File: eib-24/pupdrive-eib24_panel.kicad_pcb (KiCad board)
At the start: 2 copper layers, 125 x 110 mm, 454 parts, among them J1 050702422, J2 050702422

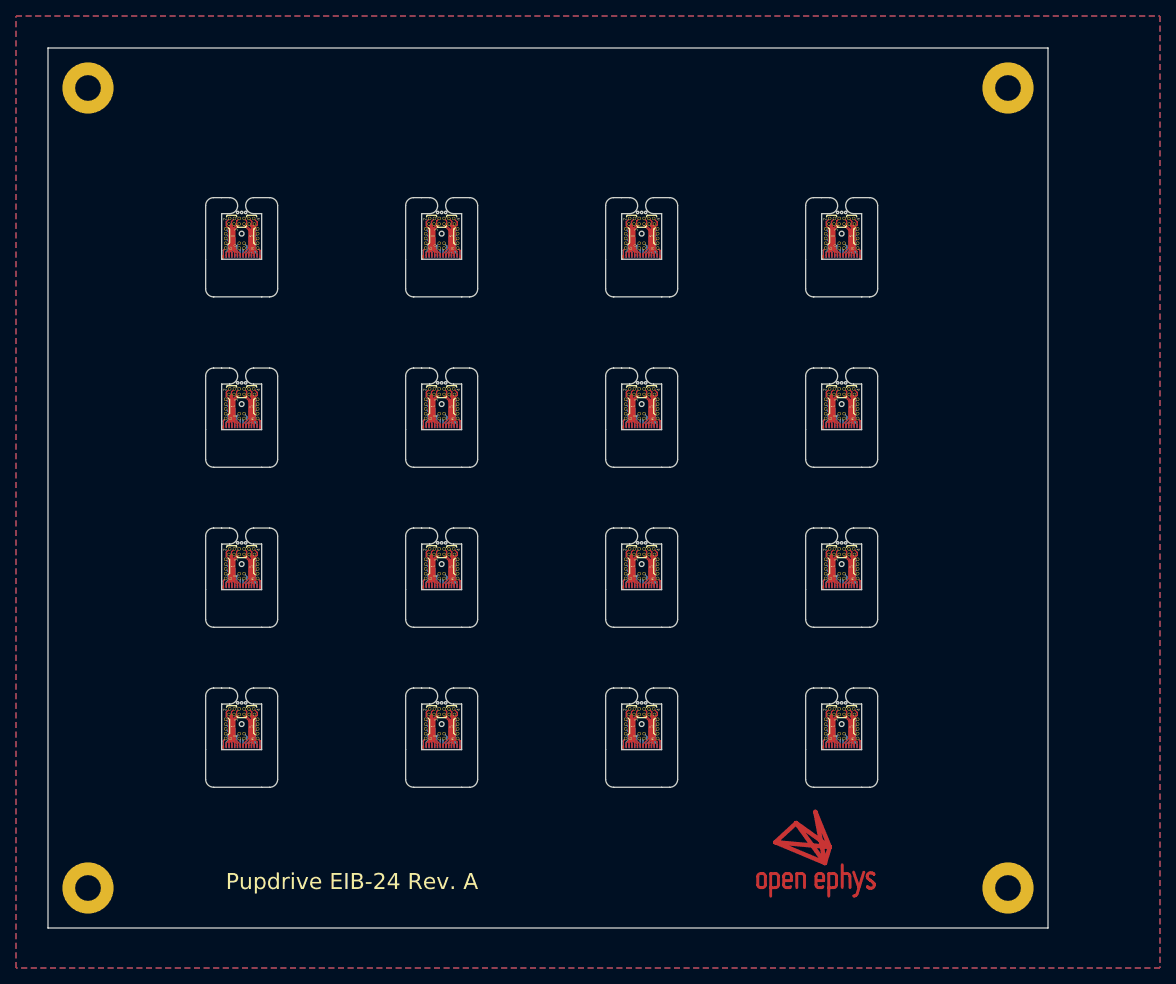
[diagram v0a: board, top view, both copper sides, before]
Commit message: Changes following first real-world test
- EIB revision B that allows it to be screwed into EIB holder for
assembly
- Small changes to drive design
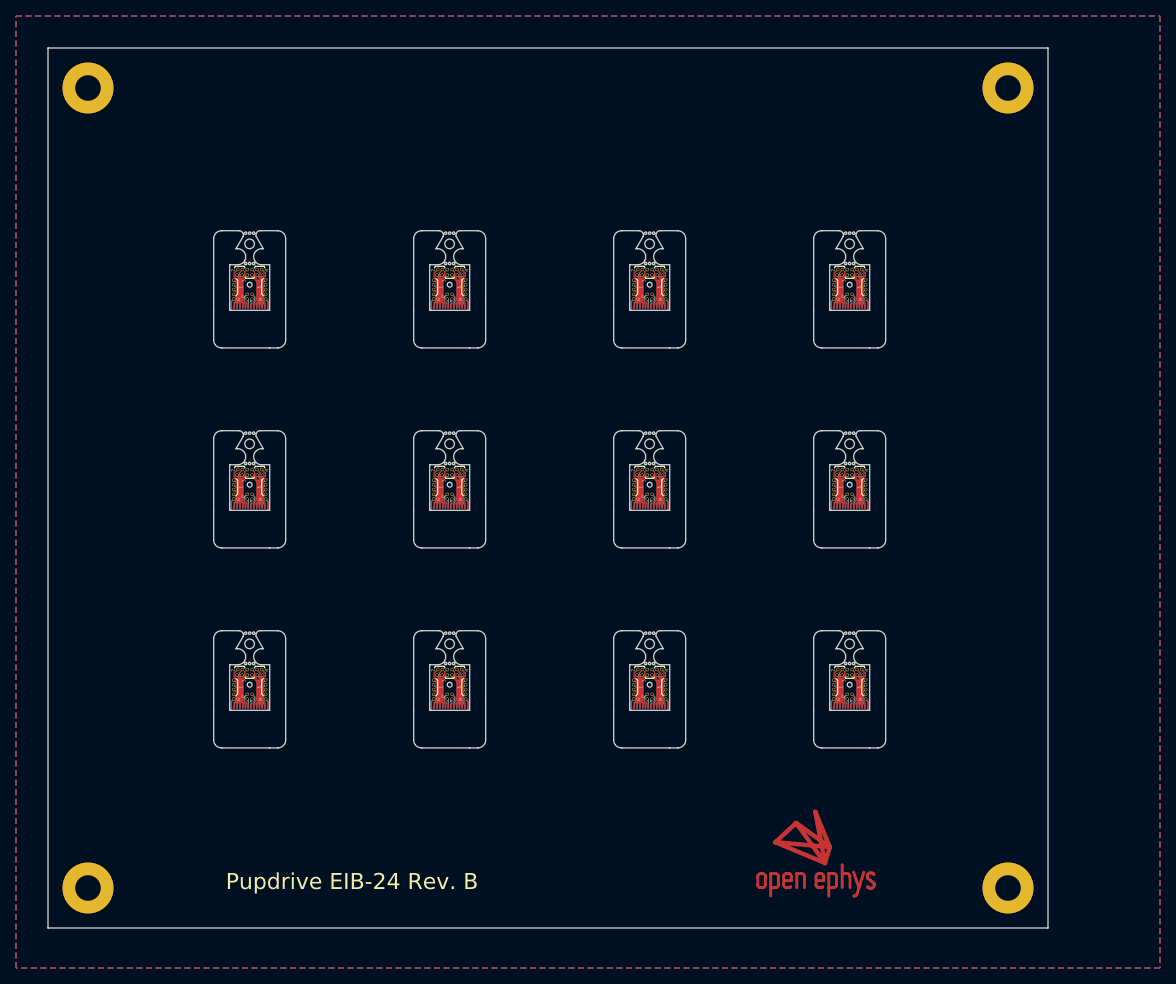
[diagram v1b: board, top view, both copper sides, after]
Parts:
- removed the J1 at (169.7, 83.9)
- removed the J1 at (119.7, 83.9)
- removed the J1 at (169.7, 62.6)
- removed the J1 at (169.7, 103.9)
- removed the J1 at (94.7, 103.9)
- removed the J1 at (119.7, 62.6)
- removed the J1 at (144.7, 103.9)
- removed the J1 at (94.7, 62.6)
- removed the J1 at (94.7, 83.9)
- removed the J1 at (144.7, 62.6)
- removed the J1 at (119.7, 103.9)
- removed the J1 at (144.7, 83.9)
- removed the J2 at (94.7, 83.9)
- removed the J2 at (144.7, 62.6)
- removed the J2 at (94.7, 103.9)
- removed the J2 at (144.7, 83.9)
- removed the J2 at (119.7, 83.9)
- removed the J2 at (119.7, 103.9)
- removed the J2 at (169.7, 62.6)
- removed the J2 at (119.7, 62.6)
- removed the J2 at (144.7, 103.9)
- removed the J2 at (94.7, 62.6)
- removed the J2 at (169.7, 83.9)
- removed the J2 at (169.7, 103.9)
- removed the TP1 at (146.7, 81.4)
- removed the TP1 at (171.7, 101.4)
- removed the TP1 at (121.7, 81.4)
- removed the TP1 at (96.7, 81.4)
- removed the TP1 at (171.7, 81.4)
- removed the TP1 at (146.7, 101.4)
- removed the TP1 at (96.7, 101.4)
- removed the TP1 at (121.7, 60.1)
- removed the TP1 at (171.7, 60.1)
- removed the TP1 at (121.7, 101.4)
- removed the TP1 at (96.7, 60.1)
- removed the TP1 at (146.7, 60.1)
- removed the TP10 at (120.0, 60.1)
- removed the TP10 at (145.0, 81.4)
- removed the TP10 at (170.0, 60.1)
- removed the TP10 at (145.0, 60.1)
- removed the TP10 at (120.0, 81.4)
- removed the TP10 at (95.0, 81.4)
- removed the TP10 at (145.0, 101.4)
- removed the TP10 at (95.0, 101.4)
- removed the TP10 at (170.0, 81.4)
- removed the TP10 at (120.0, 101.4)
- removed the TP10 at (95.0, 60.1)
- removed the TP10 at (170.0, 101.4)
- removed the TP11 at (145.0, 98.3)
- removed the TP11 at (120.0, 98.3)
- removed the TP11 at (95.0, 57.0)
- removed the TP11 at (120.0, 57.0)
- removed the TP11 at (170.0, 78.3)
- removed the TP11 at (95.0, 98.3)
- removed the TP11 at (95.0, 78.3)
- removed the TP11 at (120.0, 78.3)
- removed the TP11 at (145.0, 78.3)
- removed the TP11 at (170.0, 57.0)
- removed the TP11 at (170.0, 98.3)
- removed the TP11 at (145.0, 57.0)
- removed the TP12 at (145.0, 82.0)
- removed the TP12 at (120.0, 60.7)
- removed the TP12 at (95.0, 102.0)
- removed the TP12 at (170.0, 82.0)
- removed the TP12 at (95.0, 82.0)
- removed the TP12 at (145.0, 102.0)
- removed the TP12 at (95.0, 60.7)
- removed the TP12 at (120.0, 82.0)
- removed the TP12 at (120.0, 102.0)
- removed the TP12 at (170.0, 102.0)
- removed the TP12 at (170.0, 60.7)
- removed the TP12 at (145.0, 60.7)
- removed the TP13 at (170.0, 57.7)
- removed the TP13 at (170.0, 99.0)
- removed the TP13 at (95.0, 57.7)
- removed the TP13 at (170.0, 79.0)
- removed the TP13 at (120.0, 57.7)
- removed the TP13 at (95.0, 99.0)
- removed the TP13 at (120.0, 99.0)
- removed the TP13 at (145.0, 79.0)
- removed the TP13 at (95.0, 79.0)
- removed the TP13 at (145.0, 99.0)
- removed the TP13 at (120.0, 79.0)
- removed the TP13 at (145.0, 57.7)
- removed the TP14 at (144.4, 60.7)
- removed the TP14 at (119.4, 82.0)
- removed the TP14 at (144.4, 102.0)
- removed the TP14 at (169.4, 102.0)
- removed the TP14 at (94.4, 102.0)
- removed the TP14 at (169.4, 82.0)
- removed the TP14 at (119.4, 102.0)
- removed the TP14 at (94.4, 60.7)
- removed the TP14 at (94.4, 82.0)
- removed the TP14 at (119.4, 60.7)
- removed the TP14 at (169.4, 60.7)
- removed the TP14 at (144.4, 82.0)
- removed the TP15 at (119.4, 57.7)
- removed the TP15 at (169.4, 79.0)
- removed the TP15 at (144.4, 57.7)
- removed the TP15 at (119.4, 79.0)
- removed the TP15 at (119.4, 99.0)
- removed the TP15 at (94.4, 79.0)
- removed the TP15 at (94.4, 99.0)
- removed the TP15 at (94.4, 57.7)
- removed the TP15 at (144.4, 99.0)
- removed the TP15 at (169.4, 99.0)
- removed the TP15 at (169.4, 57.7)
- removed the TP15 at (144.4, 79.0)
- removed the TP16 at (119.4, 101.4)
- removed the TP16 at (119.4, 81.4)
- removed the TP16 at (144.4, 101.4)
- removed the TP16 at (94.4, 101.4)
- removed the TP16 at (144.4, 81.4)
- removed the TP16 at (144.4, 60.1)
- removed the TP16 at (94.4, 81.4)
- removed the TP16 at (119.4, 60.1)
- removed the TP16 at (169.4, 81.4)
- removed the TP16 at (169.4, 101.4)
- removed the TP16 at (94.4, 60.1)
- removed the TP16 at (169.4, 60.1)
- removed the TP17 at (144.4, 98.3)
- removed the TP17 at (119.4, 78.3)
- removed the TP17 at (94.4, 78.3)
- removed the TP17 at (94.4, 57.0)
- removed the TP17 at (144.4, 57.0)
- removed the TP17 at (169.4, 98.3)
- removed the TP17 at (169.4, 57.0)
- removed the TP17 at (94.4, 98.3)
- removed the TP17 at (144.4, 78.3)
- removed the TP17 at (119.4, 98.3)
- removed the TP17 at (169.4, 78.3)
- removed the TP17 at (119.4, 57.0)
- removed the TP18 at (92.7, 58.3)
- removed the TP18 at (117.7, 99.6)
- removed the TP18 at (92.7, 99.6)
- removed the TP18 at (117.7, 79.6)
- removed the TP18 at (167.7, 79.6)
- removed the TP18 at (142.7, 79.6)
- removed the TP18 at (92.7, 79.6)
- removed the TP18 at (117.7, 58.3)
- removed the TP18 at (142.7, 99.6)
- removed the TP18 at (167.7, 58.3)
- removed the TP18 at (167.7, 99.6)
- removed the TP18 at (142.7, 58.3)
- removed the TP19 at (143.8, 79.0)
- removed the TP19 at (168.8, 99.0)
- removed the TP19 at (168.8, 57.7)
- removed the TP19 at (118.8, 99.0)
- removed the TP19 at (93.8, 79.0)
- removed the TP19 at (168.8, 79.0)
- removed the TP19 at (93.8, 99.0)
- removed the TP19 at (93.8, 57.7)
- removed the TP19 at (118.8, 79.0)
- removed the TP19 at (143.8, 99.0)
- removed the TP19 at (118.8, 57.7)
- removed the TP19 at (143.8, 57.7)
- removed the TP2 at (121.7, 100.8)
- removed the TP2 at (146.7, 80.8)
- removed the TP2 at (96.7, 59.5)
- removed the TP2 at (171.7, 80.8)
- removed the TP2 at (171.7, 100.8)
- removed the TP2 at (96.7, 100.8)
- removed the TP2 at (121.7, 80.8)
- removed the TP2 at (171.7, 59.5)
- removed the TP2 at (96.7, 80.8)
- removed the TP2 at (146.7, 59.5)
- removed the TP2 at (146.7, 100.8)
- removed the TP2 at (121.7, 59.5)
- removed the TP20 at (117.7, 80.2)
- removed the TP20 at (167.7, 58.9)
- removed the TP20 at (167.7, 100.2)
- removed the TP20 at (142.7, 80.2)
- removed the TP20 at (117.7, 100.2)
- removed the TP20 at (167.7, 80.2)
- removed the TP20 at (92.7, 58.9)
- removed the TP20 at (92.7, 80.2)
- removed the TP20 at (92.7, 100.2)
- removed the TP20 at (142.7, 100.2)
- removed the TP20 at (117.7, 58.9)
- removed the TP20 at (142.7, 58.9)
- removed the TP21 at (143.8, 57.0)
- removed the TP21 at (143.8, 78.3)
- removed the TP21 at (93.8, 78.3)
- removed the TP21 at (93.8, 57.0)
- removed the TP21 at (118.8, 57.0)
- removed the TP21 at (168.8, 57.0)
- removed the TP21 at (143.8, 98.3)
- removed the TP21 at (168.8, 98.3)
- removed the TP21 at (118.8, 98.3)
- removed the TP21 at (168.8, 78.3)
- removed the TP21 at (118.8, 78.3)
- removed the TP21 at (93.8, 98.3)
- removed the TP22 at (117.7, 80.8)
- removed the TP22 at (167.7, 59.5)
- removed the TP22 at (142.7, 80.8)
- removed the TP22 at (117.7, 59.5)
- removed the TP22 at (167.7, 80.8)
- removed the TP22 at (92.7, 100.8)
- removed the TP22 at (92.7, 80.8)
- removed the TP22 at (92.7, 59.5)
- removed the TP22 at (167.7, 100.8)
- removed the TP22 at (142.7, 59.5)
- removed the TP22 at (142.7, 100.8)
- removed the TP22 at (117.7, 100.8)
- removed the TP23 at (143.1, 99.0)
- removed the TP23 at (118.1, 79.0)
- removed the TP23 at (168.1, 57.7)
- removed the TP23 at (93.1, 79.0)
- removed the TP23 at (143.1, 79.0)
- removed the TP23 at (168.1, 99.0)
- removed the TP23 at (143.1, 57.7)
- removed the TP23 at (93.1, 57.7)
- removed the TP23 at (118.1, 57.7)
- removed the TP23 at (118.1, 99.0)
- removed the TP23 at (168.1, 79.0)
- removed the TP23 at (93.1, 99.0)
- removed the TP24 at (92.7, 60.1)
- removed the TP24 at (92.7, 101.4)
- removed the TP24 at (142.7, 60.1)
- removed the TP24 at (167.7, 81.4)
- removed the TP24 at (92.7, 81.4)
- removed the TP24 at (167.7, 101.4)
- removed the TP24 at (142.7, 101.4)
- removed the TP24 at (117.7, 81.4)
- removed the TP24 at (117.7, 60.1)
- removed the TP24 at (167.7, 60.1)
- removed the TP24 at (117.7, 101.4)
- removed the TP24 at (142.7, 81.4)
- removed the TP25 at (168.2, 57.0)
- removed the TP25 at (168.2, 98.3)
- removed the TP25 at (143.2, 98.3)
- removed the TP25 at (143.2, 78.3)
- removed the TP25 at (93.2, 57.0)
- removed the TP25 at (93.2, 98.3)
- removed the TP25 at (118.2, 78.3)
- removed the TP25 at (118.2, 98.3)
- removed the TP25 at (143.2, 57.0)
- removed the TP25 at (118.2, 57.0)
- removed the TP25 at (168.2, 78.3)
- removed the TP25 at (93.2, 78.3)
- removed the TP26 at (117.7, 102.0)
- removed the TP26 at (92.7, 102.0)
- removed the TP26 at (142.7, 82.0)
- removed the TP26 at (92.7, 82.0)
- removed the TP26 at (167.7, 60.7)
- removed the TP26 at (142.7, 60.7)
- removed the TP26 at (167.7, 82.0)
- removed the TP26 at (142.7, 102.0)
- removed the TP26 at (92.7, 60.7)
- removed the TP26 at (167.7, 102.0)
- removed the TP26 at (117.7, 60.7)
- removed the TP26 at (117.7, 82.0)
- removed the TP3 at (96.7, 58.9)
- removed the TP3 at (171.7, 58.9)
- removed the TP3 at (96.7, 100.2)
- removed the TP3 at (146.7, 58.9)
- removed the TP3 at (96.7, 80.2)
- removed the TP3 at (146.7, 80.2)
- removed the TP3 at (171.7, 100.2)
- removed the TP3 at (146.7, 100.2)
- removed the TP3 at (171.7, 80.2)
- removed the TP3 at (121.7, 58.9)
- removed the TP3 at (121.7, 100.2)
- removed the TP3 at (121.7, 80.2)
- removed the TP4 at (121.7, 102.0)
- removed the TP4 at (96.7, 60.7)
- removed the TP4 at (146.7, 102.0)
- removed the TP4 at (121.7, 82.0)
- removed the TP4 at (121.7, 60.7)
- removed the TP4 at (146.7, 82.0)
- removed the TP4 at (146.7, 60.7)
- removed the TP4 at (171.7, 102.0)
- removed the TP4 at (96.7, 82.0)
- removed the TP4 at (171.7, 82.0)
- removed the TP4 at (96.7, 102.0)
- removed the TP4 at (171.7, 60.7)
- removed the TP5 at (121.2, 98.3)
- removed the TP5 at (96.2, 78.3)
- removed the TP5 at (171.2, 98.3)
- removed the TP5 at (171.2, 78.3)
- removed the TP5 at (146.2, 78.3)
- removed the TP5 at (146.2, 57.0)
- removed the TP5 at (146.2, 98.3)
- removed the TP5 at (96.2, 98.3)
- removed the TP5 at (96.2, 57.0)
- removed the TP5 at (121.2, 57.0)
- removed the TP5 at (121.2, 78.3)
- removed the TP5 at (171.2, 57.0)
- removed the TP6 at (121.3, 79.0)
- removed the TP6 at (96.3, 57.7)
- removed the TP6 at (146.3, 57.7)
- removed the TP6 at (146.3, 99.0)
- removed the TP6 at (171.3, 99.0)
- removed the TP6 at (171.3, 57.7)
- removed the TP6 at (171.3, 79.0)
- removed the TP6 at (96.3, 79.0)
- removed the TP6 at (121.3, 57.7)
- removed the TP6 at (96.3, 99.0)
- removed the TP6 at (146.3, 79.0)
- removed the TP6 at (121.3, 99.0)
- removed the TP7 at (170.6, 98.3)
- removed the TP7 at (170.6, 57.0)
- removed the TP7 at (95.6, 78.3)
- removed the TP7 at (145.6, 98.3)
- removed the TP7 at (145.6, 57.0)
- removed the TP7 at (95.6, 98.3)
- removed the TP7 at (95.6, 57.0)
- removed the TP7 at (170.6, 78.3)
- removed the TP7 at (120.6, 78.3)
- removed the TP7 at (120.6, 98.3)
- removed the TP7 at (120.6, 57.0)
- removed the TP7 at (145.6, 78.3)
- removed the TP8 at (96.7, 99.6)
- removed the TP8 at (121.7, 99.6)
- removed the TP8 at (171.7, 58.3)
- removed the TP8 at (146.7, 99.6)
- removed the TP8 at (96.7, 58.3)
- removed the TP8 at (96.7, 79.6)
- removed the TP8 at (146.7, 58.3)
- removed the TP8 at (121.7, 79.6)
- removed the TP8 at (146.7, 79.6)
- removed the TP8 at (121.7, 58.3)
- removed the TP8 at (171.7, 99.6)
- removed the TP8 at (171.7, 79.6)
- removed the TP9 at (95.7, 79.0)
- removed the TP9 at (145.7, 57.7)
- removed the TP9 at (95.7, 57.7)
- removed the TP9 at (170.7, 79.0)
- removed the TP9 at (120.7, 57.7)
- removed the TP9 at (145.7, 79.0)
- removed the TP9 at (120.7, 99.0)
- removed the TP9 at (170.7, 99.0)
- removed the TP9 at (120.7, 79.0)
- removed the TP9 at (145.7, 99.0)
- removed the TP9 at (170.7, 57.7)
- removed the TP9 at (95.7, 99.0)
- added J1: 050702422, jonnew:MOLEX_5050702422, F.Cu at (120.7, 94.0)
- added J1: 050702422, jonnew:MOLEX_5050702422, F.Cu at (95.7, 94.0)
- added J1: 050702422, jonnew:MOLEX_5050702422, F.Cu at (170.7, 94.0)
- added J1: 050702422, jonnew:MOLEX_5050702422, F.Cu at (145.7, 94.0)
- added J1: 050702422, jonnew:MOLEX_5050702422, F.Cu at (120.7, 69.0)
- added J1: 050702422, jonnew:MOLEX_5050702422, F.Cu at (170.7, 69.0)
- added J1: 050702422, jonnew:MOLEX_5050702422, F.Cu at (95.7, 69.0)
- added J1: 050702422, jonnew:MOLEX_5050702422, F.Cu at (145.7, 69.0)
- added J2: 050702422, jonnew:MOLEX_5050702422, B.Cu at (120.7, 69.0)
- added J2: 050702422, jonnew:MOLEX_5050702422, B.Cu at (170.7, 69.0)
- added J2: 050702422, jonnew:MOLEX_5050702422, B.Cu at (95.7, 94.0)
- added J2: 050702422, jonnew:MOLEX_5050702422, B.Cu at (145.7, 69.0)
- added J2: 050702422, jonnew:MOLEX_5050702422, B.Cu at (95.7, 69.0)
- added J2: 050702422, jonnew:MOLEX_5050702422, B.Cu at (145.7, 94.0)
- added J2: 050702422, jonnew:MOLEX_5050702422, B.Cu at (170.7, 94.0)
- added J2: 050702422, jonnew:MOLEX_5050702422, B.Cu at (120.7, 94.0)
- added TP1: TestPoint, jonnew:NEURALYNX_SMALL-GOLD-PIN, F.Cu at (147.7, 91.5)
- added TP1: TestPoint, jonnew:NEURALYNX_SMALL-GOLD-PIN, F.Cu at (172.7, 91.5)
- added TP1: TestPoint, jonnew:NEURALYNX_SMALL-GOLD-PIN, F.Cu at (122.7, 66.5)
- added TP1: TestPoint, jonnew:NEURALYNX_SMALL-GOLD-PIN, F.Cu at (147.7, 66.5)
- added TP1: TestPoint, jonnew:NEURALYNX_SMALL-GOLD-PIN, F.Cu at (97.7, 91.5)
- added TP1: TestPoint, jonnew:NEURALYNX_SMALL-GOLD-PIN, F.Cu at (122.7, 91.5)
- added TP1: TestPoint, jonnew:NEURALYNX_SMALL-GOLD-PIN, F.Cu at (172.7, 66.5)
- added TP1: TestPoint, jonnew:NEURALYNX_SMALL-GOLD-PIN, F.Cu at (97.7, 66.5)
- added TP10: TestPoint, jonnew:NEURALYNX_SMALL-GOLD-PIN, F.Cu at (96.0, 66.5)
- added TP10: TestPoint, jonnew:NEURALYNX_SMALL-GOLD-PIN, F.Cu at (121.0, 66.5)
- added TP10: TestPoint, jonnew:NEURALYNX_SMALL-GOLD-PIN, F.Cu at (171.0, 91.5)
- added TP10: TestPoint, jonnew:NEURALYNX_SMALL-GOLD-PIN, F.Cu at (96.0, 91.5)
- added TP10: TestPoint, jonnew:NEURALYNX_SMALL-GOLD-PIN, F.Cu at (146.0, 91.5)
- added TP10: TestPoint, jonnew:NEURALYNX_SMALL-GOLD-PIN, F.Cu at (121.0, 91.5)
- added TP10: TestPoint, jonnew:NEURALYNX_SMALL-GOLD-PIN, F.Cu at (171.0, 66.5)
- added TP10: TestPoint, jonnew:NEURALYNX_SMALL-GOLD-PIN, F.Cu at (146.0, 66.5)
- added TP11: TestPoint, jonnew:NEURALYNX_SMALL-GOLD-PIN, F.Cu at (171.0, 63.4)
- added TP11: TestPoint, jonnew:NEURALYNX_SMALL-GOLD-PIN, F.Cu at (121.0, 88.4)
- added TP11: TestPoint, jonnew:NEURALYNX_SMALL-GOLD-PIN, F.Cu at (121.0, 63.4)
- added TP11: TestPoint, jonnew:NEURALYNX_SMALL-GOLD-PIN, F.Cu at (146.0, 88.4)
- added TP11: TestPoint, jonnew:NEURALYNX_SMALL-GOLD-PIN, F.Cu at (146.0, 63.4)
- added TP11: TestPoint, jonnew:NEURALYNX_SMALL-GOLD-PIN, F.Cu at (96.0, 63.4)
- added TP11: TestPoint, jonnew:NEURALYNX_SMALL-GOLD-PIN, F.Cu at (96.0, 88.4)
- added TP11: TestPoint, jonnew:NEURALYNX_SMALL-GOLD-PIN, F.Cu at (171.0, 88.4)
- added TP12: TestPoint, jonnew:NEURALYNX_SMALL-GOLD-PIN, F.Cu at (121.0, 92.1)
- added TP12: TestPoint, jonnew:NEURALYNX_SMALL-GOLD-PIN, F.Cu at (121.0, 67.1)
- added TP12: TestPoint, jonnew:NEURALYNX_SMALL-GOLD-PIN, F.Cu at (96.0, 67.1)
- added TP12: TestPoint, jonnew:NEURALYNX_SMALL-GOLD-PIN, F.Cu at (146.0, 92.1)
- added TP12: TestPoint, jonnew:NEURALYNX_SMALL-GOLD-PIN, F.Cu at (171.0, 67.1)
- added TP12: TestPoint, jonnew:NEURALYNX_SMALL-GOLD-PIN, F.Cu at (146.0, 67.1)
- added TP12: TestPoint, jonnew:NEURALYNX_SMALL-GOLD-PIN, F.Cu at (96.0, 92.1)
- added TP12: TestPoint, jonnew:NEURALYNX_SMALL-GOLD-PIN, F.Cu at (171.0, 92.1)
- added TP13: TestPoint, jonnew:NEURALYNX_SMALL-GOLD-PIN, F.Cu at (96.0, 64.1)
- added TP13: TestPoint, jonnew:NEURALYNX_SMALL-GOLD-PIN, F.Cu at (121.0, 89.1)
- added TP13: TestPoint, jonnew:NEURALYNX_SMALL-GOLD-PIN, F.Cu at (146.0, 89.1)
- added TP13: TestPoint, jonnew:NEURALYNX_SMALL-GOLD-PIN, F.Cu at (171.0, 64.1)
- added TP13: TestPoint, jonnew:NEURALYNX_SMALL-GOLD-PIN, F.Cu at (121.0, 64.1)
- added TP13: TestPoint, jonnew:NEURALYNX_SMALL-GOLD-PIN, F.Cu at (146.0, 64.1)
- added TP13: TestPoint, jonnew:NEURALYNX_SMALL-GOLD-PIN, F.Cu at (96.0, 89.1)
- added TP13: TestPoint, jonnew:NEURALYNX_SMALL-GOLD-PIN, F.Cu at (171.0, 89.1)
- added TP14: TestPoint, jonnew:NEURALYNX_SMALL-GOLD-PIN, F.Cu at (145.4, 92.1)
- added TP14: TestPoint, jonnew:NEURALYNX_SMALL-GOLD-PIN, F.Cu at (170.4, 67.1)
- added TP14: TestPoint, jonnew:NEURALYNX_SMALL-GOLD-PIN, F.Cu at (145.4, 67.1)
- added TP14: TestPoint, jonnew:NEURALYNX_SMALL-GOLD-PIN, F.Cu at (120.4, 67.1)
- added TP14: TestPoint, jonnew:NEURALYNX_SMALL-GOLD-PIN, F.Cu at (95.4, 92.1)
- added TP14: TestPoint, jonnew:NEURALYNX_SMALL-GOLD-PIN, F.Cu at (120.4, 92.1)
- added TP14: TestPoint, jonnew:NEURALYNX_SMALL-GOLD-PIN, F.Cu at (170.4, 92.1)
- added TP14: TestPoint, jonnew:NEURALYNX_SMALL-GOLD-PIN, F.Cu at (95.4, 67.1)
- added TP15: TestPoint, jonnew:NEURALYNX_SMALL-GOLD-PIN, F.Cu at (120.4, 89.1)
- added TP15: TestPoint, jonnew:NEURALYNX_SMALL-GOLD-PIN, F.Cu at (145.4, 64.1)
- added TP15: TestPoint, jonnew:NEURALYNX_SMALL-GOLD-PIN, F.Cu at (170.4, 64.1)
- added TP15: TestPoint, jonnew:NEURALYNX_SMALL-GOLD-PIN, F.Cu at (95.4, 89.1)
- added TP15: TestPoint, jonnew:NEURALYNX_SMALL-GOLD-PIN, F.Cu at (95.4, 64.1)
- added TP15: TestPoint, jonnew:NEURALYNX_SMALL-GOLD-PIN, F.Cu at (120.4, 64.1)
- added TP15: TestPoint, jonnew:NEURALYNX_SMALL-GOLD-PIN, F.Cu at (145.4, 89.1)
- added TP15: TestPoint, jonnew:NEURALYNX_SMALL-GOLD-PIN, F.Cu at (170.4, 89.1)
- added TP16: TestPoint, jonnew:NEURALYNX_SMALL-GOLD-PIN, F.Cu at (170.4, 66.5)
- added TP16: TestPoint, jonnew:NEURALYNX_SMALL-GOLD-PIN, F.Cu at (120.4, 91.5)
- added TP16: TestPoint, jonnew:NEURALYNX_SMALL-GOLD-PIN, F.Cu at (95.4, 66.5)
- added TP16: TestPoint, jonnew:NEURALYNX_SMALL-GOLD-PIN, F.Cu at (145.4, 66.5)
- added TP16: TestPoint, jonnew:NEURALYNX_SMALL-GOLD-PIN, F.Cu at (170.4, 91.5)
- added TP16: TestPoint, jonnew:NEURALYNX_SMALL-GOLD-PIN, F.Cu at (95.4, 91.5)
- added TP16: TestPoint, jonnew:NEURALYNX_SMALL-GOLD-PIN, F.Cu at (145.4, 91.5)
- added TP16: TestPoint, jonnew:NEURALYNX_SMALL-GOLD-PIN, F.Cu at (120.4, 66.5)
- added TP17: TestPoint, jonnew:NEURALYNX_SMALL-GOLD-PIN, F.Cu at (95.4, 63.4)
- added TP17: TestPoint, jonnew:NEURALYNX_SMALL-GOLD-PIN, F.Cu at (120.4, 88.4)
- added TP17: TestPoint, jonnew:NEURALYNX_SMALL-GOLD-PIN, F.Cu at (170.4, 88.4)
- added TP17: TestPoint, jonnew:NEURALYNX_SMALL-GOLD-PIN, F.Cu at (145.4, 88.4)
- added TP17: TestPoint, jonnew:NEURALYNX_SMALL-GOLD-PIN, F.Cu at (95.4, 88.4)
- added TP17: TestPoint, jonnew:NEURALYNX_SMALL-GOLD-PIN, F.Cu at (120.4, 63.4)
- added TP17: TestPoint, jonnew:NEURALYNX_SMALL-GOLD-PIN, F.Cu at (145.4, 63.4)
- added TP17: TestPoint, jonnew:NEURALYNX_SMALL-GOLD-PIN, F.Cu at (170.4, 63.4)
- added TP18: TestPoint, jonnew:NEURALYNX_SMALL-GOLD-PIN, F.Cu at (143.7, 64.7)
- added TP18: TestPoint, jonnew:NEURALYNX_SMALL-GOLD-PIN, F.Cu at (118.7, 64.7)
- added TP18: TestPoint, jonnew:NEURALYNX_SMALL-GOLD-PIN, F.Cu at (118.7, 89.7)
- added TP18: TestPoint, jonnew:NEURALYNX_SMALL-GOLD-PIN, F.Cu at (168.7, 64.7)
- added TP18: TestPoint, jonnew:NEURALYNX_SMALL-GOLD-PIN, F.Cu at (93.7, 64.7)
- added TP18: TestPoint, jonnew:NEURALYNX_SMALL-GOLD-PIN, F.Cu at (93.7, 89.7)
- added TP18: TestPoint, jonnew:NEURALYNX_SMALL-GOLD-PIN, F.Cu at (143.7, 89.7)
- added TP18: TestPoint, jonnew:NEURALYNX_SMALL-GOLD-PIN, F.Cu at (168.7, 89.7)
- added TP19: TestPoint, jonnew:NEURALYNX_SMALL-GOLD-PIN, F.Cu at (169.8, 64.1)
- added TP19: TestPoint, jonnew:NEURALYNX_SMALL-GOLD-PIN, F.Cu at (144.8, 64.1)
- added TP19: TestPoint, jonnew:NEURALYNX_SMALL-GOLD-PIN, F.Cu at (144.8, 89.1)
- added TP19: TestPoint, jonnew:NEURALYNX_SMALL-GOLD-PIN, F.Cu at (94.8, 64.1)
- added TP19: TestPoint, jonnew:NEURALYNX_SMALL-GOLD-PIN, F.Cu at (119.8, 64.1)
- added TP19: TestPoint, jonnew:NEURALYNX_SMALL-GOLD-PIN, F.Cu at (169.8, 89.1)
- added TP19: TestPoint, jonnew:NEURALYNX_SMALL-GOLD-PIN, F.Cu at (94.8, 89.1)
- added TP19: TestPoint, jonnew:NEURALYNX_SMALL-GOLD-PIN, F.Cu at (119.8, 89.1)
- added TP2: TestPoint, jonnew:NEURALYNX_SMALL-GOLD-PIN, F.Cu at (172.7, 65.9)
- added TP2: TestPoint, jonnew:NEURALYNX_SMALL-GOLD-PIN, F.Cu at (97.7, 65.9)
- added TP2: TestPoint, jonnew:NEURALYNX_SMALL-GOLD-PIN, F.Cu at (97.7, 90.9)
- added TP2: TestPoint, jonnew:NEURALYNX_SMALL-GOLD-PIN, F.Cu at (147.7, 90.9)
- added TP2: TestPoint, jonnew:NEURALYNX_SMALL-GOLD-PIN, F.Cu at (122.7, 90.9)
- added TP2: TestPoint, jonnew:NEURALYNX_SMALL-GOLD-PIN, F.Cu at (122.7, 65.9)
- added TP2: TestPoint, jonnew:NEURALYNX_SMALL-GOLD-PIN, F.Cu at (147.7, 65.9)
- added TP2: TestPoint, jonnew:NEURALYNX_SMALL-GOLD-PIN, F.Cu at (172.7, 90.9)
- added TP20: TestPoint, jonnew:NEURALYNX_SMALL-GOLD-PIN, F.Cu at (168.7, 90.3)
- added TP20: TestPoint, jonnew:NEURALYNX_SMALL-GOLD-PIN, F.Cu at (168.7, 65.3)
- added TP20: TestPoint, jonnew:NEURALYNX_SMALL-GOLD-PIN, F.Cu at (118.7, 90.3)
- added TP20: TestPoint, jonnew:NEURALYNX_SMALL-GOLD-PIN, F.Cu at (93.7, 65.3)
- added TP20: TestPoint, jonnew:NEURALYNX_SMALL-GOLD-PIN, F.Cu at (143.7, 90.3)
- added TP20: TestPoint, jonnew:NEURALYNX_SMALL-GOLD-PIN, F.Cu at (93.7, 90.3)
- added TP20: TestPoint, jonnew:NEURALYNX_SMALL-GOLD-PIN, F.Cu at (118.7, 65.3)
- added TP20: TestPoint, jonnew:NEURALYNX_SMALL-GOLD-PIN, F.Cu at (143.7, 65.3)
- added TP21: TestPoint, jonnew:NEURALYNX_SMALL-GOLD-PIN, F.Cu at (144.8, 63.4)
- added TP21: TestPoint, jonnew:NEURALYNX_SMALL-GOLD-PIN, F.Cu at (119.8, 63.4)
- added TP21: TestPoint, jonnew:NEURALYNX_SMALL-GOLD-PIN, F.Cu at (119.8, 88.4)
- added TP21: TestPoint, jonnew:NEURALYNX_SMALL-GOLD-PIN, F.Cu at (94.8, 88.4)
- added TP21: TestPoint, jonnew:NEURALYNX_SMALL-GOLD-PIN, F.Cu at (169.8, 88.4)
- added TP21: TestPoint, jonnew:NEURALYNX_SMALL-GOLD-PIN, F.Cu at (169.8, 63.4)
- added TP21: TestPoint, jonnew:NEURALYNX_SMALL-GOLD-PIN, F.Cu at (144.8, 88.4)
- added TP21: TestPoint, jonnew:NEURALYNX_SMALL-GOLD-PIN, F.Cu at (94.8, 63.4)
- added TP22: TestPoint, jonnew:NEURALYNX_SMALL-GOLD-PIN, F.Cu at (93.7, 90.9)
- added TP22: TestPoint, jonnew:NEURALYNX_SMALL-GOLD-PIN, F.Cu at (143.7, 65.9)
- added TP22: TestPoint, jonnew:NEURALYNX_SMALL-GOLD-PIN, F.Cu at (168.7, 65.9)
- added TP22: TestPoint, jonnew:NEURALYNX_SMALL-GOLD-PIN, F.Cu at (118.7, 90.9)
- added TP22: TestPoint, jonnew:NEURALYNX_SMALL-GOLD-PIN, F.Cu at (168.7, 90.9)
- added TP22: TestPoint, jonnew:NEURALYNX_SMALL-GOLD-PIN, F.Cu at (93.7, 65.9)
- added TP22: TestPoint, jonnew:NEURALYNX_SMALL-GOLD-PIN, F.Cu at (118.7, 65.9)
- added TP22: TestPoint, jonnew:NEURALYNX_SMALL-GOLD-PIN, F.Cu at (143.7, 90.9)
- added TP23: TestPoint, jonnew:NEURALYNX_SMALL-GOLD-PIN, F.Cu at (169.1, 89.1)
- added TP23: TestPoint, jonnew:NEURALYNX_SMALL-GOLD-PIN, F.Cu at (144.1, 89.1)
- added TP23: TestPoint, jonnew:NEURALYNX_SMALL-GOLD-PIN, F.Cu at (94.1, 64.1)
- added TP23: TestPoint, jonnew:NEURALYNX_SMALL-GOLD-PIN, F.Cu at (144.1, 64.1)
- added TP23: TestPoint, jonnew:NEURALYNX_SMALL-GOLD-PIN, F.Cu at (169.1, 64.1)
- added TP23: TestPoint, jonnew:NEURALYNX_SMALL-GOLD-PIN, F.Cu at (119.1, 89.1)
- added TP23: TestPoint, jonnew:NEURALYNX_SMALL-GOLD-PIN, F.Cu at (119.1, 64.1)
- added TP23: TestPoint, jonnew:NEURALYNX_SMALL-GOLD-PIN, F.Cu at (94.1, 89.1)
- added TP24: TestPoint, jonnew:NEURALYNX_SMALL-GOLD-PIN, F.Cu at (143.7, 66.5)
- added TP24: TestPoint, jonnew:NEURALYNX_SMALL-GOLD-PIN, F.Cu at (93.7, 91.5)
- added TP24: TestPoint, jonnew:NEURALYNX_SMALL-GOLD-PIN, F.Cu at (168.7, 91.5)
- added TP24: TestPoint, jonnew:NEURALYNX_SMALL-GOLD-PIN, F.Cu at (93.7, 66.5)
- added TP24: TestPoint, jonnew:NEURALYNX_SMALL-GOLD-PIN, F.Cu at (118.7, 66.5)
- added TP24: TestPoint, jonnew:NEURALYNX_SMALL-GOLD-PIN, F.Cu at (118.7, 91.5)
- added TP24: TestPoint, jonnew:NEURALYNX_SMALL-GOLD-PIN, F.Cu at (143.7, 91.5)
- added TP24: TestPoint, jonnew:NEURALYNX_SMALL-GOLD-PIN, F.Cu at (168.7, 66.5)
- added TP25: TestPoint, jonnew:NEURALYNX_SMALL-GOLD-PIN, F.Cu at (169.2, 88.4)
- added TP25: TestPoint, jonnew:NEURALYNX_SMALL-GOLD-PIN, F.Cu at (94.2, 88.4)
- added TP25: TestPoint, jonnew:NEURALYNX_SMALL-GOLD-PIN, F.Cu at (144.2, 88.4)
- added TP25: TestPoint, jonnew:NEURALYNX_SMALL-GOLD-PIN, F.Cu at (94.2, 63.4)
- added TP25: TestPoint, jonnew:NEURALYNX_SMALL-GOLD-PIN, F.Cu at (119.2, 88.4)
- added TP25: TestPoint, jonnew:NEURALYNX_SMALL-GOLD-PIN, F.Cu at (119.2, 63.4)
- added TP25: TestPoint, jonnew:NEURALYNX_SMALL-GOLD-PIN, F.Cu at (169.2, 63.4)
- added TP25: TestPoint, jonnew:NEURALYNX_SMALL-GOLD-PIN, F.Cu at (144.2, 63.4)
- added TP26: TestPoint, jonnew:NEURALYNX_SMALL-GOLD-PIN, F.Cu at (143.7, 67.1)
- added TP26: TestPoint, jonnew:NEURALYNX_SMALL-GOLD-PIN, F.Cu at (168.7, 67.1)
- added TP26: TestPoint, jonnew:NEURALYNX_SMALL-GOLD-PIN, F.Cu at (93.7, 92.1)
- added TP26: TestPoint, jonnew:NEURALYNX_SMALL-GOLD-PIN, F.Cu at (168.7, 92.1)
- added TP26: TestPoint, jonnew:NEURALYNX_SMALL-GOLD-PIN, F.Cu at (118.7, 67.1)
- added TP26: TestPoint, jonnew:NEURALYNX_SMALL-GOLD-PIN, F.Cu at (93.7, 67.1)
- added TP26: TestPoint, jonnew:NEURALYNX_SMALL-GOLD-PIN, F.Cu at (118.7, 92.1)
- added TP26: TestPoint, jonnew:NEURALYNX_SMALL-GOLD-PIN, F.Cu at (143.7, 92.1)
- added TP3: TestPoint, jonnew:NEURALYNX_SMALL-GOLD-PIN, F.Cu at (147.7, 65.3)
- added TP3: TestPoint, jonnew:NEURALYNX_SMALL-GOLD-PIN, F.Cu at (147.7, 90.3)
- added TP3: TestPoint, jonnew:NEURALYNX_SMALL-GOLD-PIN, F.Cu at (122.7, 90.3)
- added TP3: TestPoint, jonnew:NEURALYNX_SMALL-GOLD-PIN, F.Cu at (172.7, 90.3)
- added TP3: TestPoint, jonnew:NEURALYNX_SMALL-GOLD-PIN, F.Cu at (97.7, 65.3)
- added TP3: TestPoint, jonnew:NEURALYNX_SMALL-GOLD-PIN, F.Cu at (122.7, 65.3)
- added TP3: TestPoint, jonnew:NEURALYNX_SMALL-GOLD-PIN, F.Cu at (97.7, 90.3)
- added TP3: TestPoint, jonnew:NEURALYNX_SMALL-GOLD-PIN, F.Cu at (172.7, 65.3)
- added TP4: TestPoint, jonnew:NEURALYNX_SMALL-GOLD-PIN, F.Cu at (122.7, 67.1)
- added TP4: TestPoint, jonnew:NEURALYNX_SMALL-GOLD-PIN, F.Cu at (147.7, 92.1)
- added TP4: TestPoint, jonnew:NEURALYNX_SMALL-GOLD-PIN, F.Cu at (147.7, 67.1)
- added TP4: TestPoint, jonnew:NEURALYNX_SMALL-GOLD-PIN, F.Cu at (172.7, 92.1)
- added TP4: TestPoint, jonnew:NEURALYNX_SMALL-GOLD-PIN, F.Cu at (97.7, 67.1)
- added TP4: TestPoint, jonnew:NEURALYNX_SMALL-GOLD-PIN, F.Cu at (97.7, 92.1)
- added TP4: TestPoint, jonnew:NEURALYNX_SMALL-GOLD-PIN, F.Cu at (172.7, 67.1)
- added TP4: TestPoint, jonnew:NEURALYNX_SMALL-GOLD-PIN, F.Cu at (122.7, 92.1)
- added TP5: TestPoint, jonnew:NEURALYNX_SMALL-GOLD-PIN, F.Cu at (97.2, 63.4)
- added TP5: TestPoint, jonnew:NEURALYNX_SMALL-GOLD-PIN, F.Cu at (147.2, 63.4)
- added TP5: TestPoint, jonnew:NEURALYNX_SMALL-GOLD-PIN, F.Cu at (147.2, 88.4)
- added TP5: TestPoint, jonnew:NEURALYNX_SMALL-GOLD-PIN, F.Cu at (172.2, 63.4)
- added TP5: TestPoint, jonnew:NEURALYNX_SMALL-GOLD-PIN, F.Cu at (172.2, 88.4)
- added TP5: TestPoint, jonnew:NEURALYNX_SMALL-GOLD-PIN, F.Cu at (122.2, 63.4)
- added TP5: TestPoint, jonnew:NEURALYNX_SMALL-GOLD-PIN, F.Cu at (122.2, 88.4)
- added TP5: TestPoint, jonnew:NEURALYNX_SMALL-GOLD-PIN, F.Cu at (97.2, 88.4)
- added TP6: TestPoint, jonnew:NEURALYNX_SMALL-GOLD-PIN, F.Cu at (122.3, 64.1)
- added TP6: TestPoint, jonnew:NEURALYNX_SMALL-GOLD-PIN, F.Cu at (172.3, 89.1)
- added TP6: TestPoint, jonnew:NEURALYNX_SMALL-GOLD-PIN, F.Cu at (147.3, 89.1)
- added TP6: TestPoint, jonnew:NEURALYNX_SMALL-GOLD-PIN, F.Cu at (147.3, 64.1)
- added TP6: TestPoint, jonnew:NEURALYNX_SMALL-GOLD-PIN, F.Cu at (122.3, 89.1)
- added TP6: TestPoint, jonnew:NEURALYNX_SMALL-GOLD-PIN, F.Cu at (97.3, 89.1)
- added TP6: TestPoint, jonnew:NEURALYNX_SMALL-GOLD-PIN, F.Cu at (97.3, 64.1)
- added TP6: TestPoint, jonnew:NEURALYNX_SMALL-GOLD-PIN, F.Cu at (172.3, 64.1)
- added TP7: TestPoint, jonnew:NEURALYNX_SMALL-GOLD-PIN, F.Cu at (96.6, 63.4)
- added TP7: TestPoint, jonnew:NEURALYNX_SMALL-GOLD-PIN, F.Cu at (146.6, 88.4)
- added TP7: TestPoint, jonnew:NEURALYNX_SMALL-GOLD-PIN, F.Cu at (146.6, 63.4)
- added TP7: TestPoint, jonnew:NEURALYNX_SMALL-GOLD-PIN, F.Cu at (171.6, 88.4)
- added TP7: TestPoint, jonnew:NEURALYNX_SMALL-GOLD-PIN, F.Cu at (121.6, 88.4)
- added TP7: TestPoint, jonnew:NEURALYNX_SMALL-GOLD-PIN, F.Cu at (171.6, 63.4)
- added TP7: TestPoint, jonnew:NEURALYNX_SMALL-GOLD-PIN, F.Cu at (121.6, 63.4)
- added TP7: TestPoint, jonnew:NEURALYNX_SMALL-GOLD-PIN, F.Cu at (96.6, 88.4)
- added TP8: TestPoint, jonnew:NEURALYNX_SMALL-GOLD-PIN, F.Cu at (147.7, 89.7)
- added TP8: TestPoint, jonnew:NEURALYNX_SMALL-GOLD-PIN, F.Cu at (172.7, 89.7)
- added TP8: TestPoint, jonnew:NEURALYNX_SMALL-GOLD-PIN, F.Cu at (97.7, 64.7)
- added TP8: TestPoint, jonnew:NEURALYNX_SMALL-GOLD-PIN, F.Cu at (147.7, 64.7)
- added TP8: TestPoint, jonnew:NEURALYNX_SMALL-GOLD-PIN, F.Cu at (172.7, 64.7)
- added TP8: TestPoint, jonnew:NEURALYNX_SMALL-GOLD-PIN, F.Cu at (122.7, 89.7)
- added TP8: TestPoint, jonnew:NEURALYNX_SMALL-GOLD-PIN, F.Cu at (122.7, 64.7)
- added TP8: TestPoint, jonnew:NEURALYNX_SMALL-GOLD-PIN, F.Cu at (97.7, 89.7)
- added TP9: TestPoint, jonnew:NEURALYNX_SMALL-GOLD-PIN, F.Cu at (96.7, 89.1)
- added TP9: TestPoint, jonnew:NEURALYNX_SMALL-GOLD-PIN, F.Cu at (146.7, 89.1)
- added TP9: TestPoint, jonnew:NEURALYNX_SMALL-GOLD-PIN, F.Cu at (171.7, 64.1)
- added TP9: TestPoint, jonnew:NEURALYNX_SMALL-GOLD-PIN, F.Cu at (171.7, 89.1)
- added TP9: TestPoint, jonnew:NEURALYNX_SMALL-GOLD-PIN, F.Cu at (121.7, 64.1)
- added TP9: TestPoint, jonnew:NEURALYNX_SMALL-GOLD-PIN, F.Cu at (121.7, 89.1)
- added TP9: TestPoint, jonnew:NEURALYNX_SMALL-GOLD-PIN, F.Cu at (96.7, 64.1)
- added TP9: TestPoint, jonnew:NEURALYNX_SMALL-GOLD-PIN, F.Cu at (146.7, 64.1)
- moved J1 5.02 mm to (120.7, 119.0)
- moved J1 5.02 mm to (95.7, 119.0)
- moved J2 5.02 mm to (95.7, 119.0)
- moved J2 5.02 mm to (120.7, 119.0)
- moved TP1 5.02 mm to (97.7, 116.5)
- moved TP1 5.02 mm to (122.7, 116.5)
- moved TP10 5.02 mm to (146.0, 116.5)
- moved TP10 5.02 mm to (171.0, 116.5)
- moved TP11 5.02 mm to (146.0, 113.4)
- moved TP11 5.02 mm to (171.0, 113.4)
- moved TP12 5.02 mm to (146.0, 117.1)
- moved TP12 5.02 mm to (171.0, 117.1)
- moved TP13 5.02 mm to (171.0, 114.1)
- moved TP13 5.02 mm to (146.0, 114.1)
- moved TP14 5.02 mm to (95.4, 117.1)
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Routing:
- net /E5: track 83.7 -> 62.8 mm
- net /E8: track 82.7 -> 62.0 mm
- net /E12: track 82.1 -> 61.6 mm
- net /E1: track 81.5 -> 61.1 mm
- net /E3: track 79.1 -> 59.4 mm
- net /E10: track 78.1 -> 58.6 mm
- net /E6: track 72.6 -> 54.5 mm
- net /E7: track 71.8 -> 53.9 mm
- net /E4: track 67.9 -> 50.9 mm
- net /E9: track 66.9 -> 50.2 mm
- net /E11: track 65.7 -> 49.3 mm
- net /E2: track 64.7 -> 48.5 mm
- net /E21: track 61.7 -> 46.3 mm
- net /E16: track 61.7 -> 46.3 mm
- net /E15: track 49.8 -> 37.3 mm
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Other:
- outline, holes or cut-outs redrawn
- board text added: "Pupdrive EIB-24 Rev. B"
- board text removed: "Pupdrive EIB-24 Rev. A"
